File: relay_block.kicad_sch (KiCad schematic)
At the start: 49 parts, among them J4 Screw_Terminal_01x02, J5 Screw_Terminal_01x10, J6 Screw_Terminal_01x10, U10 TLP3558A, U11 TLP3558A, U12 TLP3558A, U13 TLP3558A, U14 TLP3558A, U15 TLP3558A, U16 TLP3558A, U17 TLP3558A, U18 TLP3558A, U19 TLP3558A, U20 TLP3558A, U21 TLP3558A, U22 TLP3558A, U23 TLP3558A, U24 TLP3558A, U25 TLP3558A, U4 TLP3558A, U5 TLP3558A, U6 TLP3558A, U7 TLP3558A, U8 TLP3558A, U9 TLP3558A

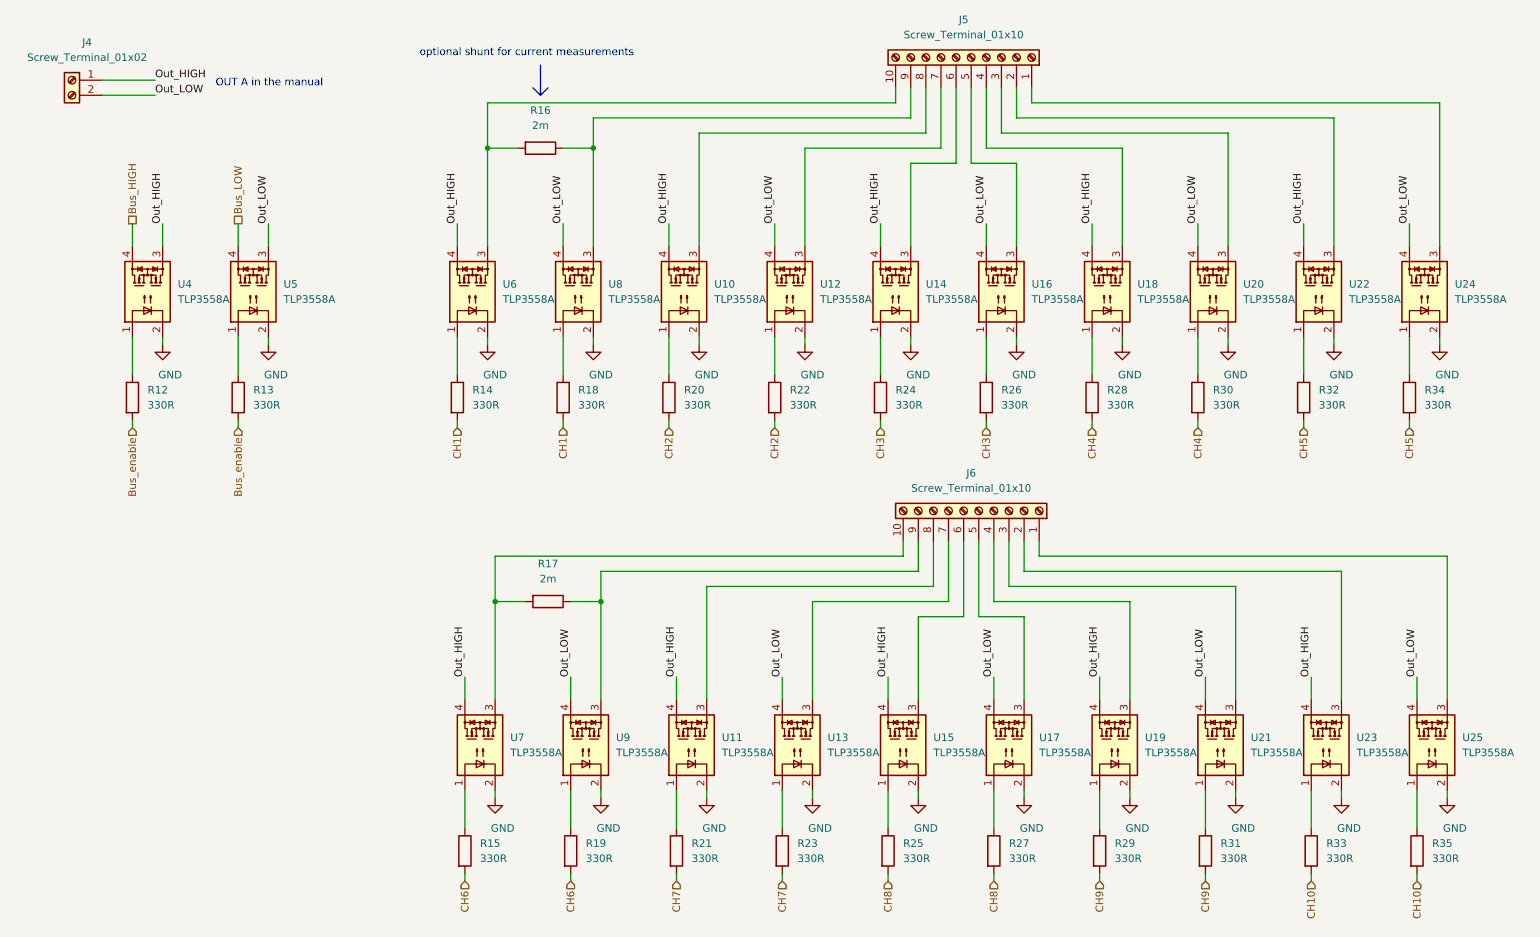
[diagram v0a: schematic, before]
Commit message: Version 1.6
Created a high-voltage rated scan board.

Control is done completely in logic to avoid programming an MCU
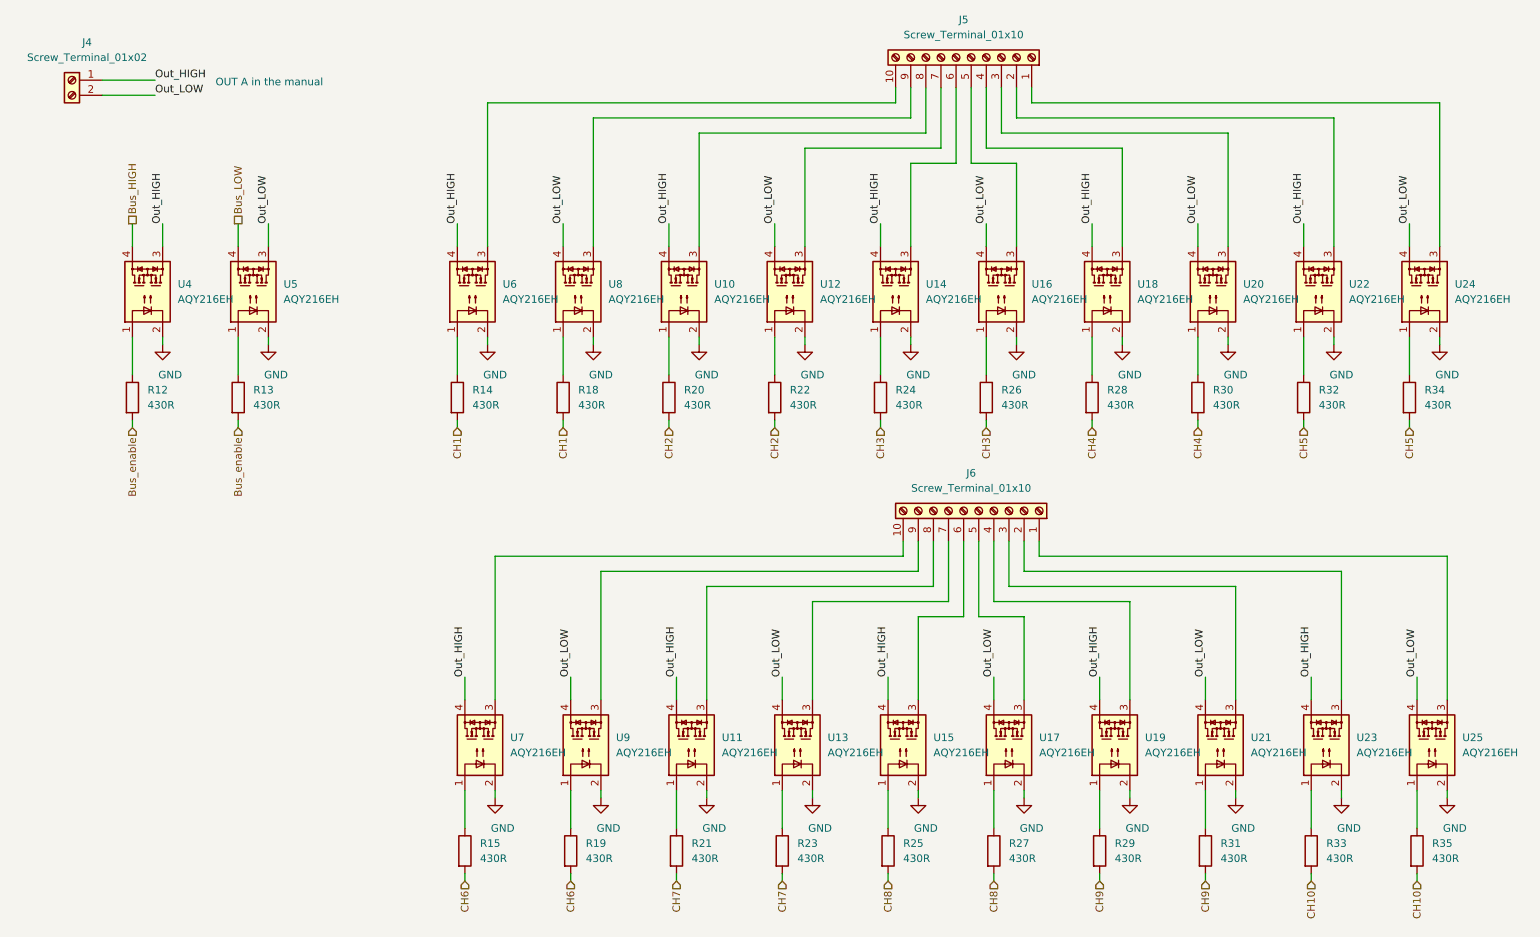
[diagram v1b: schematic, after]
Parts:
- removed R16, R17: 2m, Resistor_SMD:R_2512_6332Metric, symbol Device:R
- R12, R13, R14, R15, R18, R19, R20, R21, R22, R23, R24, R25, R26, R27, R28, R29, R30, R31, R32, R33, R34, R35: value 330R -> 430R
- U10, U11, U12, U13, U14, U15, U16, U17, U18, U19, U20, U21, U22, U23, U24, U25, U4, U5, U6, U7, U8, U9: value TLP3558A -> AQY216EH; footprint Package_DIP:DIP-4_W7.62mm -> Package_DIP:DIP-4_W7.62mm_Least
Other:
- note removed: "optional shunt for current measurements"
